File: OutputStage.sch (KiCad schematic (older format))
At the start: 58 parts, among them Q12 BSC067N06LS3, Q13 BSC067N06LS3, Q3 AON7400A, Q5 AON7400A, U5 LM5175PWPR

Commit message: Much layout wow.
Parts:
- removed C127, C40: 220u, Capacitor_SMD:C_Elec_8x10.2, symbol Device:C_Small
- added C127, C148, C149, C40: 220u, Capacitor_SMD:C_Elec_8x10.2, symbol Device:CP_Small
- added C150, C151, C152, C153, C154: 22u, lc_lib:0805_C, symbol Device:C_Small
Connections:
- wire segments 136 -> 149
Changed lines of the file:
@@
 OUTPUT_VOLTAGE
-$Comp
-L Device:C_Small C?
-U 1 1 5FF124CA
-P 1050 1250
-AR Path="/5FD99B08/5FF124CA" Ref="C?"  Part="1"
-AR Path="/60413DD6/5FF124CA" Ref="C40"  Part="1"
-F 0 "C40" H 1142 1296 50  0000 L CNN
-F 1 "220u" H 1142 1205 50  0000 L CNN
-F 2 "Capacitor_SMD:C_Elec_8x10.2" H 1050 1250 50  0001 C CNN
-F 3 "~" H 1050 1250 50  0001 C CNN
-F 4 "C311611" H 1050 1250 50  0001 C CNN "LCSC"
-	1    1050 1250
-	-1   0    0    1
-$EndComp
 $Comp
 L Connector:TestPoint TP?
@@
 Wire Wire Line
 	1050 900  1050 1150
-Connection ~ 1050 1150
-$Comp
-L SmartBattery:AO4468 Q13
-U 1 1 5FF7195E
-P 6900 1400
-F 0 "Q13" H 7106 1446 50  0000 L CNN
-F 1 "BSC067N06LS3" H 7106 1355 50  0000 L CNN
-F 2 "lc_lib:DFN-8_5X6MM" H 7100 1500 50  0001 C CNN
-F 3 "~" H 6900 1400 50  0001 C CNN
-F 4 "" H 6900 1400 50  0001 C CNN "SKU"
-F 5 "C24199" H 6900 1400 50  0001 C CNN "LCSC"
-	1    6900 1400
-	1    0    0    -1
-$EndComp
 $Comp
 L SmartBattery:AO4468 Q12
@@
 	8300 550  8300 600
 Wire Wire Line
-	7000 550  8300 550
+	7000 550  7850 550
 Wire Wire Line
 	8300 900  8300 850
@@
 Wire Wire Line
 	8300 850  8300 800
-$Comp
-L Device:C_Small C?
-U 1 1 600A063D
-P 8750 650
-AR Path="/5FD99B08/600A063D" Ref="C?"  Part="1"
-AR Path="/60413DD6/600A063D" Ref="C127"  Part="1"
-F 0 "C127" H 8842 696 50  0000 L CNN
-F 1 "220u" H 8842 605 50  0000 L CNN
-F 2 "Capacitor_SMD:C_Elec_8x10.2" H 8750 650 50  0001 C CNN
-F 3 "~" H 8750 650 50  0001 C CNN
-F 4 "C311611" H 8750 650 50  0001 C CNN "LCSC"
-	1    8750 650
-	-1   0    0    1
-$EndComp
 $Comp
 L Device:C_Small C?
@@
 	8900 750  8750 750
 Connection ~ 8900 750
-Wire Wire Line
-	8300 550  8750 550
 Connection ~ 8300 550
-Connection ~ 8750 550
-Wire Wire Line
-	8750 550  8900 550
 Connection ~ 8900 550
 Wire Wire Line
@@
 Connection ~ 9950 550
 Wire Wire Line
-	10350 550  10350 3800
+	10350 550  10350 1100
 Wire Wire Line
 	10350 3800 6300 3800
@@
 	1    0    0    -1
 $EndComp
+$Comp
+L Device:CP_Small C127
+U 1 1 600C29BE
+P 8750 650
+F 0 "C127" H 9000 700 50  0000 R CNN
+F 1 "220u" H 9000 600 50  0000 R CNN
+F 2 "Capacitor_SMD:C_Elec_8x10.2" H 8750 650 50  0001 C CNN
+F 3 "~" H 8750 650 50  0001 C CNN
+F 4 "C311611" H 8750 650 50  0001 C CNN "LCSC"
+	1    8750 650
+	-1   0    0    -1
+$EndComp
+Wire Wire Line
+	8300 550  8750 550
+Connection ~ 8750 550
+Wire Wire Line
+	8750 550  8900 550
+$Comp
+L Device:CP_Small C40
+U 1 1 600CC4E4
+P 1050 1250
+F 0 "C40" H 1300 1300 50  0000 R CNN
+F 1 "220u" H 1300 1200 50  0000 R CNN
+F 2 "Capacitor_SMD:C_Elec_8x10.2" H 1050 1250 50  0001 C CNN
+F 3 "~" H 1050 1250 50  0001 C CNN
+F 4 "C311611" H 1050 1250 50  0001 C CNN "LCSC"
+	1    1050 1250
+	-1   0    0    -1
+$EndComp
+Connection ~ 1050 1150
+$Comp
+L SmartBattery:AO4468 Q13
+U 1 1 602BB5BE
+P 6900 1400
+F 0 "Q13" H 7106 1446 50  0000 L CNN
+F 1 "BSC067N06LS3" H 7106 1355 50  0000 L CNN
+F 2 "lc_lib:DFN-8_5X6MM" H 7100 1500 50  0001 C CNN
+F 3 "~" H 6900 1400 50  0001 C CNN
+F 4 "" H 6900 1400 50  0001 C CNN "SKU"
+F 5 "C24199" H 6900 1400 50  0001 C CNN "LCSC"
+	1    6900 1400
+	1    0    0    -1
+$EndComp
+$Comp
+L Device:CP_Small C148
+U 1 1 602CBF39
+P 7850 650
+F 0 "C148" H 8100 700 50  0000 R CNN
+F 1 "220u" H 8100 600 50  0000 R CNN
+F 2 "Capacitor_SMD:C_Elec_8x10.2" H 7850 650 50  0001 C CNN
+F 3 "~" H 7850 650 50  0001 C CNN
+F 4 "C311611" H 7850 650 50  0001 C CNN "LCSC"
+	1    7850 650
+	-1   0    0    -1
+$EndComp
+Connection ~ 7850 550
+Wire Wire Line
+	7850 550  8150 550
+$Comp
+L Device:CP_Small C149
+U 1 1 602CE5D4
+P 8150 650
+F 0 "C149" H 8400 700 50  0000 R CNN
+F 1 "220u" H 8400 600 50  0000 R CNN
+F 2 "Capacitor_SMD:C_Elec_8x10.2" H 8150 650 50  0001 C CNN
+F 3 "~" H 8150 650 50  0001 C CNN
+F 4 "C311611" H 8150 650 50  0001 C CNN "LCSC"
+	1    8150 650
+	-1   0    0    -1
+$EndComp
+Connection ~ 8150 550
+Wire Wire Line
+	8150 550  8300 550
+$Comp
+L power:GND #PWR0243
+U 1 1 602CED76
+P 7850 750
+F 0 "#PWR0243" H 7850 500 50  0001 C CNN
+F 1 "GND" H 7855 577 50  0000 C CNN
+F 2 "" H 7850 750 50  0001 C CNN
+F 3 "" H 7850 750 50  0001 C CNN
+	1    7850 750
+	1    0    0    -1
+$EndComp
+$Comp
+L power:GND #PWR0244
+U 1 1 602CF1B1
+P 8150 750
+F 0 "#PWR0244" H 8150 500 50  0001 C CNN
+F 1 "GND" H 8155 577 50  0000 C CNN
+F 2 "" H 8150 750 50  0001 C CNN
+F 3 "" H 8150 750 50  0001 C CNN
+	1    8150 750
+	1    0    0    -1
+$EndComp
+$Comp
+L Device:C_Small C?
+U 1 1 602E0116
+P 9600 1200
+AR Path="/5FD99B08/602E0116" Ref="C?"  Part="1"
+AR Path="/60413DD6/602E0116" Ref="C152"  Part="1"
+F 0 "C152" H 9692 1246 50  0000 L CNN
+F 1 "22u" H 9692 1155 50  0000 L CNN
+F 2 "lc_lib:0805_C" H 9600 1200 50  0001 C CNN
+F 3 "~" H 9600 1200 50  0001 C CNN
+F 4 "C45783" H 9600 1200 50  0001 C CNN "LCSC"
+	1    9600 1200
+	1    0    0    -1
+$EndComp
+$Comp
+L Device:C_Small C?
+U 1 1 602E113D
+P 9850 1200
+AR Path="/5FD99B08/602E113D" Ref="C?"  Part="1"
+AR Path="/60413DD6/602E113D" Ref="C153"  Part="1"
+F 0 "C153" H 9942 1246 50  0000 L CNN
+F 1 "22u" H 9942 1155 50  0000 L CNN
+F 2 "lc_lib:0805_C" H 9850 1200 50  0001 C CNN
+F 3 "~" H 9850 1200 50  0001 C CNN
+F 4 "C45783" H 9850 1200 50  0001 C CNN "LCSC"
+	1    9850 1200
+	1    0    0    -1
+$EndComp
+$Comp
+L Device:C_Small C?
+U 1 1 602E15BE
+P 10100 1200
+AR Path="/5FD99B08/602E15BE" Ref="C?"  Part="1"
+AR Path="/60413DD6/602E15BE" Ref="C154"  Part="1"
+F 0 "C154" H 10192 1246 50  0000 L CNN
+F 1 "22u" H 10192 1155 50  0000 L CNN
+F 2 "lc_lib:0805_C" H 10100 1200 50  0001 C CNN
+F 3 "~" H 10100 1200 50  0001 C CNN
+F 4 "C45783" H 10100 1200 50  0001 C CNN "LCSC"
+	1    10100 1200
+	1    0    0    -1
+$EndComp
+$Comp
+L Device:C_Small C?
+U 1 1 602E1865
+P 9400 1200
+AR Path="/5FD99B08/602E1865" Ref="C?"  Part="1"
+AR Path="/60413DD6/602E1865" Ref="C151"  Part="1"
+F 0 "C151" H 9492 1246 50  0000 L CNN
+F 1 "22u" H 9492 1155 50  0000 L CNN
+F 2 "lc_lib:0805_C" H 9400 1200 50  0001 C CNN
+F 3 "~" H 9400 1200 50  0001 C CNN
+F 4 "C45783" H 9400 1200 50  0001 C CNN "LCSC"
+	1    9400 1200
+	1    0    0    -1
+$EndComp
+$Comp
+L Device:C_Small C?
+U 1 1 602E1C32
+P 9250 1200
+AR Path="/5FD99B08/602E1C32" Ref="C?"  Part="1"
+AR Path="/60413DD6/602E1C32" Ref="C150"  Part="1"
+F 0 "C150" H 9342 1246 50  0000 L CNN
+F 1 "22u" H 9342 1155 50  0000 L CNN
+F 2 "lc_lib:0805_C" H 9250 1200 50  0001 C CNN
+F 3 "~" H 9250 1200 50  0001 C CNN
+F 4 "C45783" H 9250 1200 50  0001 C CNN "LCSC"
+	1    9250 1200
+	1    0    0    -1
+$EndComp
+Wire Wire Line
+	10350 1100 10100 1100
+Connection ~ 10350 1100
+Wire Wire Line
+	10350 1100 10350 3800
+Connection ~ 9400 1100
+Wire Wire Line
+	9400 1100 9250 1100
+Connection ~ 9600 1100
+Wire Wire Line
+	9600 1100 9400 1100
+Connection ~ 9850 1100
+Wire Wire Line
+	9850 1100 9600 1100
+Connection ~ 10100 1100
+Wire Wire Line
+	10100 1100 9850 1100
+Wire Wire Line
+	9250 1300 9400 1300
+Connection ~ 9400 1300
+Wire Wire Line
+	9400 1300 9500 1300
+Connection ~ 9600 1300
+Wire Wire Line
+	9600 1300 9850 1300
+Connection ~ 9850 1300
+Wire Wire Line
+	9850 1300 10100 1300
+$Comp
+L power:GND #PWR0245
+U 1 1 602EE718
+P 9500 1300
+F 0 "#PWR0245" H 9500 1050 50  0001 C CNN
+F 1 "GND" H 9505 1127 50  0000 C CNN
+F 2 "" H 9500 1300 50  0001 C CNN
+F 3 "" H 9500 1300 50  0001 C CNN
+	1    9500 1300
+	1    0    0    -1
+$EndComp
+Connection ~ 9500 1300
+Wire Wire Line
+	9500 1300 9600 1300
 $EndSCHEMATC

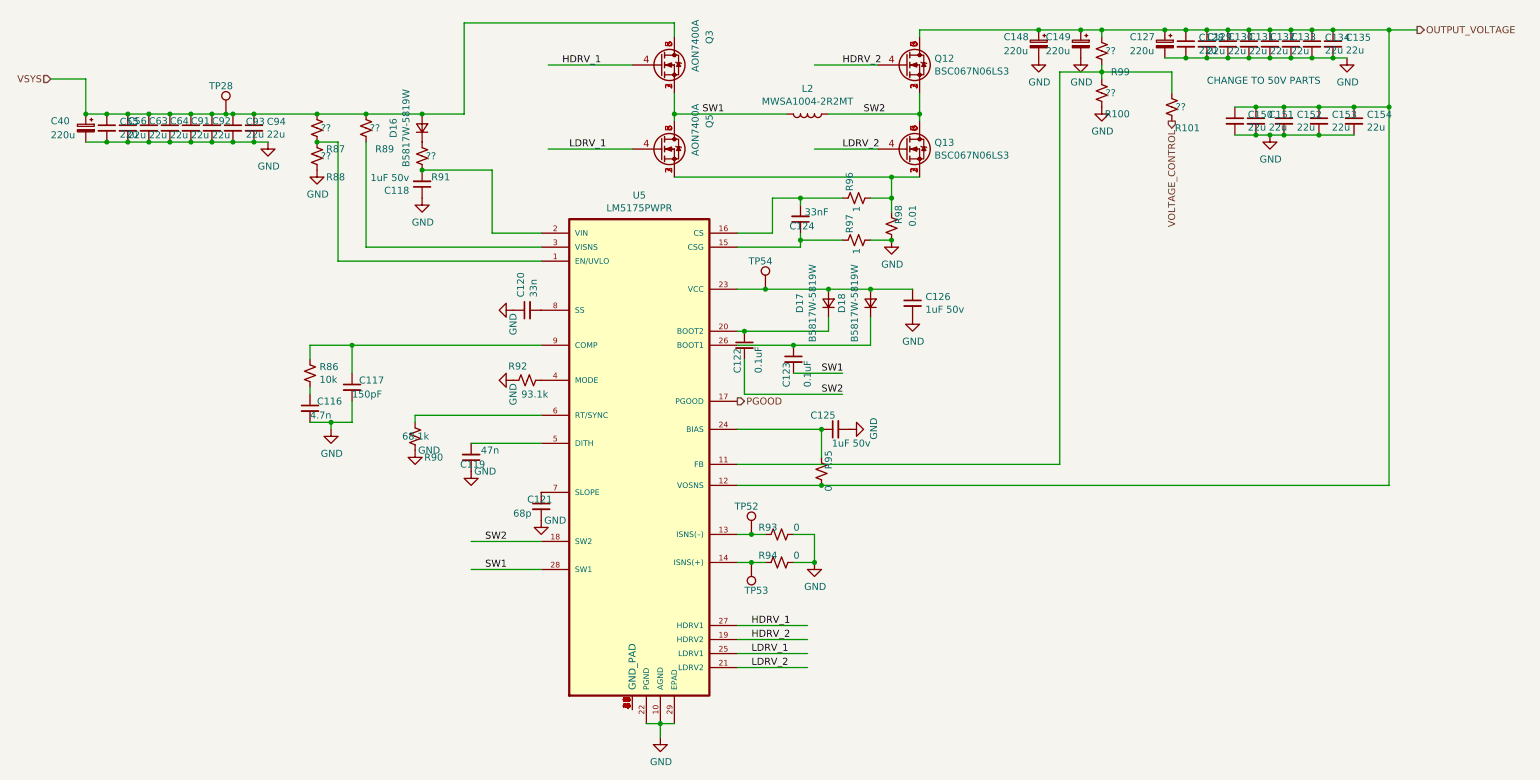
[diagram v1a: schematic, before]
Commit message: Almost connected MCU + ESP32 added leds addedd uart usb cleaned up type-c I/O -- STILL NEED TO level shift I2C
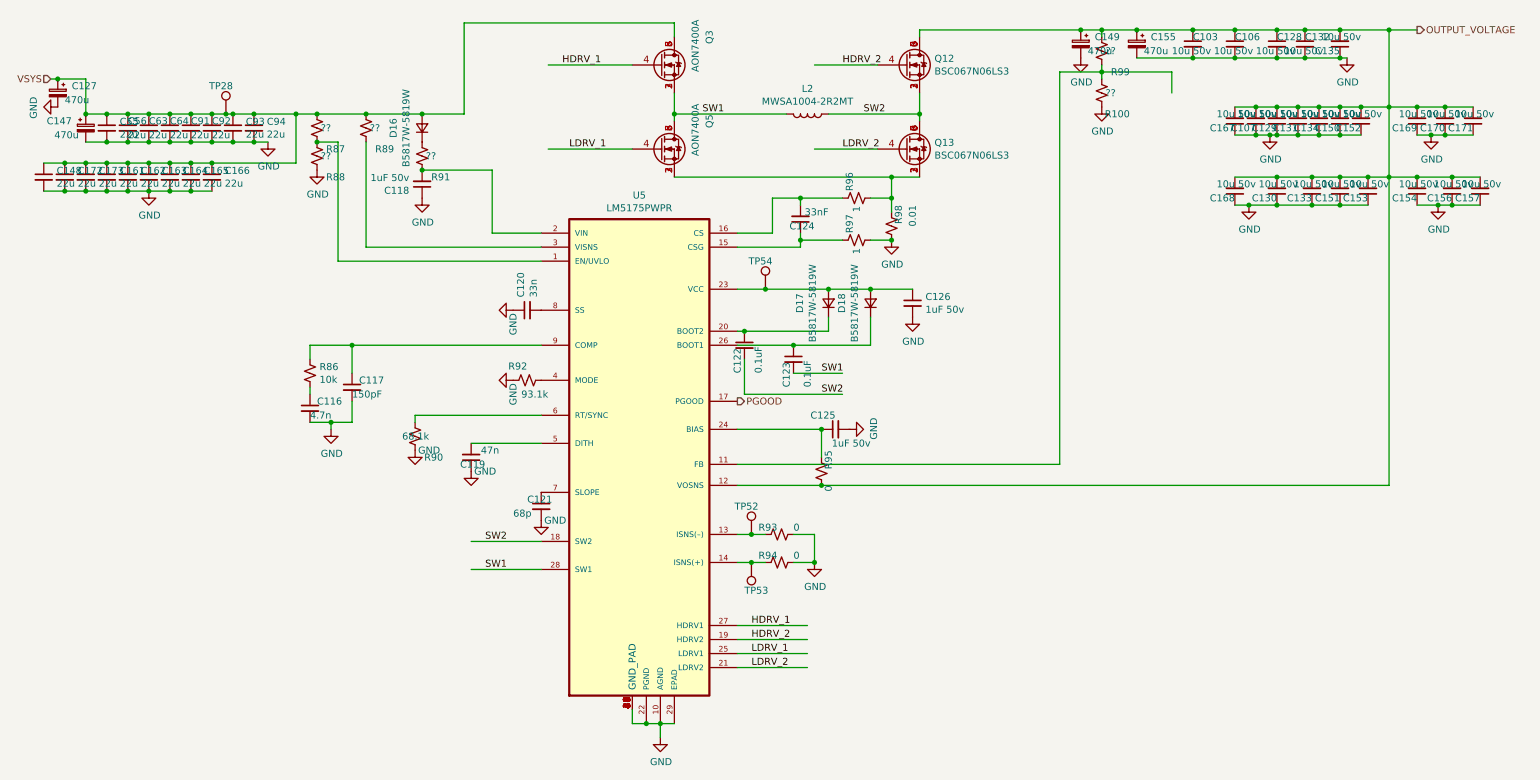
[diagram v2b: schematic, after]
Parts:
- removed C148, C40: 220u, Capacitor_SMD:C_Elec_8x10.2, symbol Device:CP_Small
- removed R101: ??, lc_lib:0402_R, symbol Device:R_Small_US
- added C103, C106, C107, C156, C157, C167, C168, C169, C170, C171: 10u 50v, lc_lib:0805_C, symbol Device:C_Small
- added C147, C155: 470u, Capacitor_SMD:C_Elec_10x10.2, symbol Device:CP_Small
- added C148, C161, C162, C163, C164, C165, C166, C172, C173: 22u, lc_lib:0805_C, symbol Device:C_Small
- C127, C149: value 220u -> 470u; footprint Capacitor_SMD:C_Elec_8x10.2 -> Capacitor_SMD:C_Elec_10x10.2; LCSC C311611 -> C72519; pn (none) -> RVT1V471M1010
- C128, C129, C130, C131, C132, C133, C134, C135, C150, C151, C152, C153, C154: value 22u -> 10u 50v; LCSC C45783 -> C13585
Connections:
- net labels removed: VOLTAGE_CONTROL
- wire segments 149 -> 191
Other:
- note removed: "CHANGE TO 50V PARTS\n"

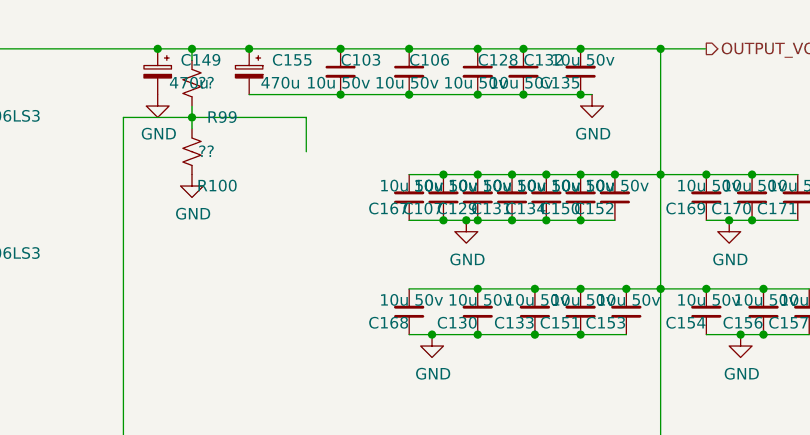
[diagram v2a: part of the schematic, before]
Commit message: lots of GPIO connectivity changes. fixed no PD on input fixed CH340G leakage. can otherwise power from GPIO. added fet for powering VCONN from 3v/5v NEED TO ADD OVERCURRENT
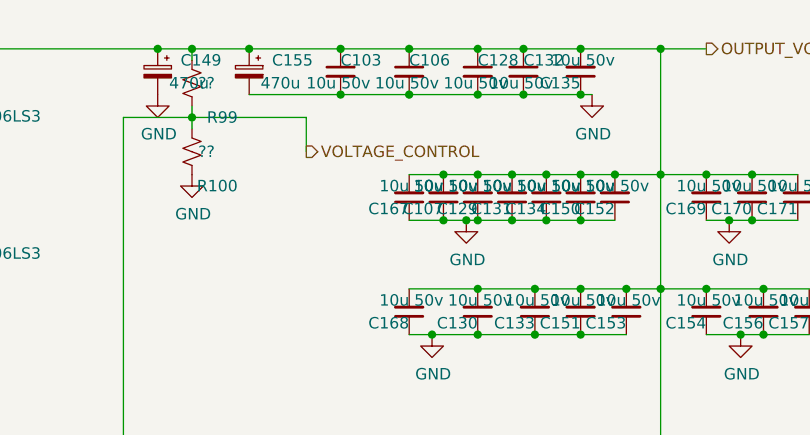
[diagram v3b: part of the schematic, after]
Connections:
- net labels added: VOLTAGE_CONTROL
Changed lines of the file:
@@
 	4950 5500 4950 5400
 Connection ~ 5050 5500
+Text HLabel 8800 1000 2    50   Output ~ 0
+VOLTAGE_CONTROL
 $EndSCHEMATC
